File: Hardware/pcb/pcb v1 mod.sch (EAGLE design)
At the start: 36 parts, among them K1 JS-M1-9V-4, K2 JS-M1-9V-4, Q1 32.768kHz 12.5pF, Q6 MOSFET-NCHANNELBSS138, Q7 MOSFET-NCHANNELBSS138, Q8 MOSFET-NCHANNELBSS138, Q9 MOSFET-NCHANNELBSS138, U1 ADP3338AKCZ-3.3RL7

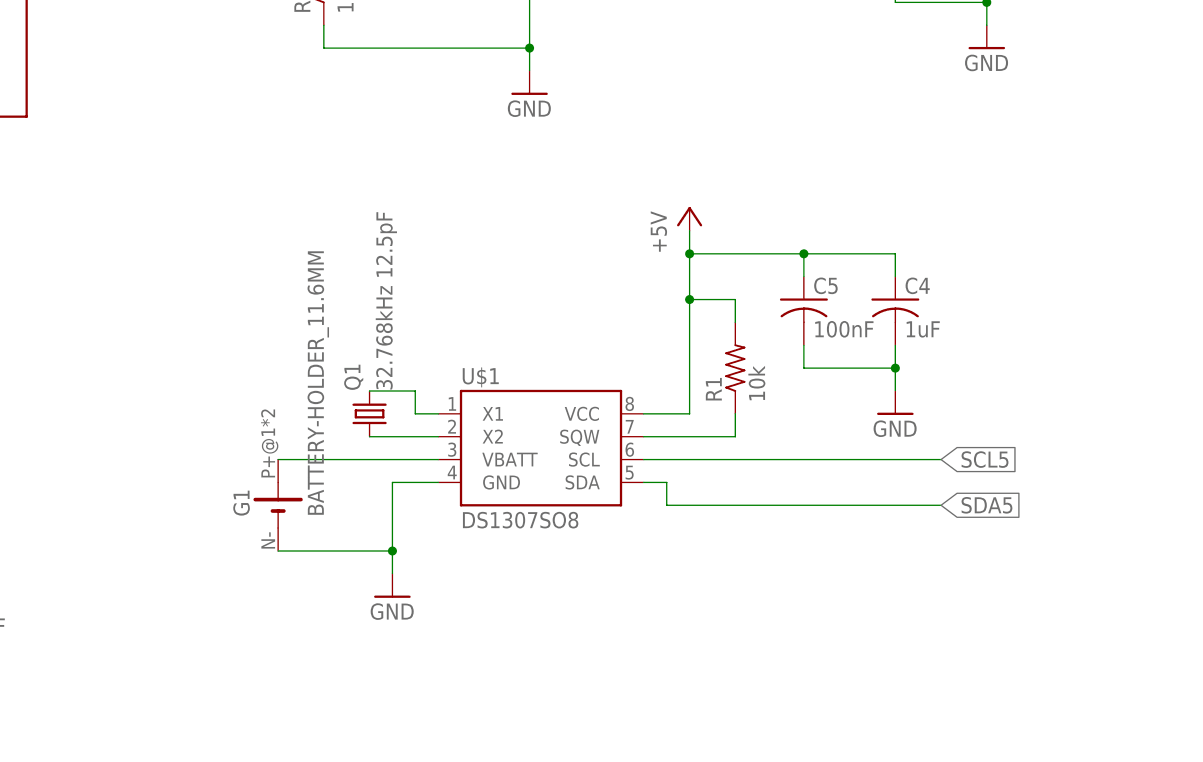
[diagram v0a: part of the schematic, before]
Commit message: Quitar el rtc
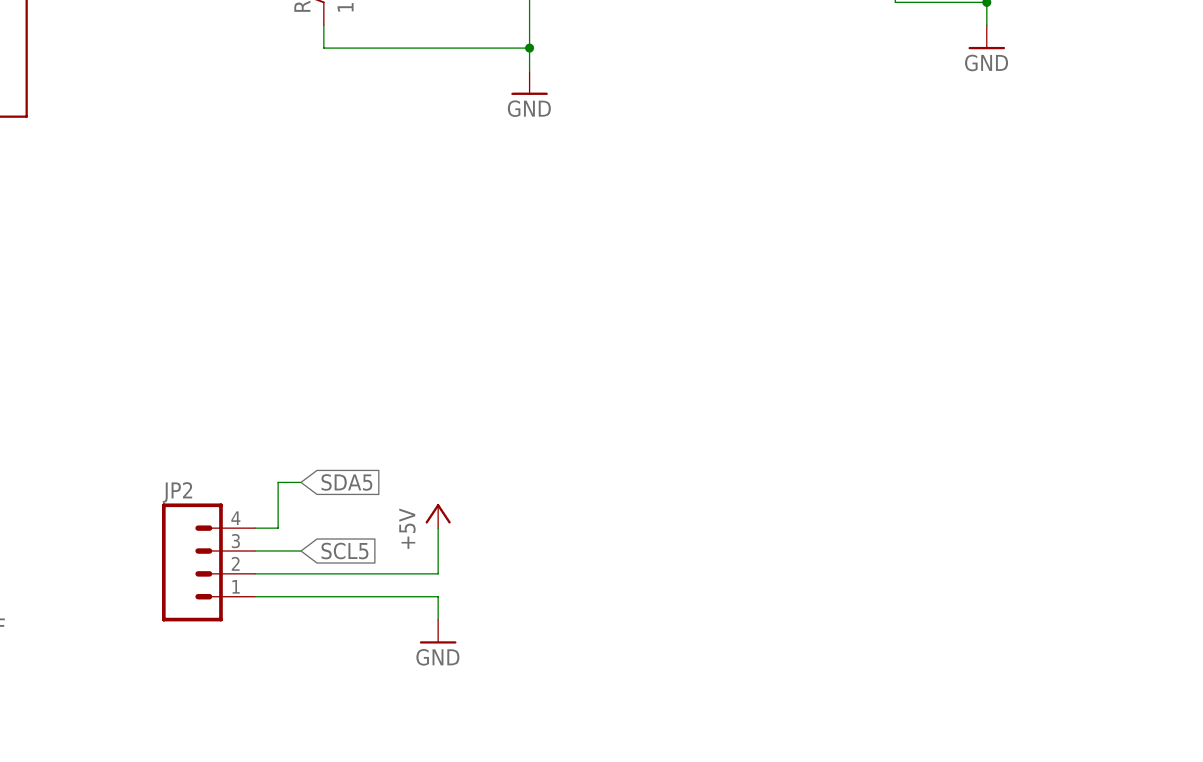
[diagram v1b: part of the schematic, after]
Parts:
- removed C4: 1uF, rcl:C-USC0805
- removed C5: 100nF, rcl:C-USC0805
- removed G1: BATTERY-HOLDER_11.6MM, battery:BATTERY-HOLDER_11.6MM
- removed Q1: 32.768kHz 12.5pF, crystal:CRYSTALTC26H
- removed R1: 10k, rcl:R-US_R0805
- removed U$1: DS1307SO8, SparkFun-FreqCtrl:DS1307SO8
- added JP2: (no value), SparkFun-Connectors:M04PTH
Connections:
- removed net N$2: Q1.2, U$1.X1
- removed net N$3: Q1.1, U$1.X2
- removed net N$4: G1.+, U$1.VBATT
- removed net N$6: R1.1, U$1.SQW
- net +5V: now also JP2.2; no longer C4.1, C5.1, R1.2, U$1.VCC
- net GND: now also JP2.1; no longer C4.2, C5.2, G1.-, U$1.GND
- net SCL5: now also JP2.3; no longer U$1.SCL
- net SDA5: now also JP2.4; no longer U$1.SDA
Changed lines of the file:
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@@
 </classes>
 <parts>
-<part name="G1" library="battery" deviceset="BATTERY-HOLDER_11.6MM" device=""/>
-<part name="Q1" library="crystal" deviceset="CRYSTAL" device="TC26H" value="32.768kHz 12.5pF"/>
 <part name="RFID1" library="partes" deviceset="GROVE-RFID" device=""/>
 <part name="MDL1" library="ESP8266-ESP12E" deviceset="ESP8266-12E" device="ESP8266-ESP12E"/>
@@
 <part name="P+1" library="supply1" deviceset="+5V" device=""/>
 <part name="S1" library="SparkFun-Electromechanical" deviceset="SWITCH-SPDT" device="PTH"/>
-<part name="U$1" library="SparkFun-FreqCtrl" deviceset="DS1307" device="SO8"/>
 <part name="P+2" library="supply1" deviceset="+5V" device=""/>
 <part name="GND3" library="supply1" deviceset="GND" device=""/>
-<part name="R1" library="rcl" deviceset="R-US_" device="R0805" value="10k"/>
 <part name="GND4" library="supply1" deviceset="GND" device=""/>
 <part name="P+6" library="supply1" deviceset="+5V" device=""/>
@@
 <part name="GND8" library="supply1" deviceset="GND" device=""/>
 <part name="GND9" library="supply1" deviceset="GND" device=""/>
-<part name="C4" library="rcl" deviceset="C-US" device="C0805" value="1uF"/>
-<part name="C5" library="rcl" deviceset="C-US" device="C0805" value="100nF"/>
-<part name="GND10" library="supply1" deviceset="GND" device=""/>
 <part name="C6" library="rcl" deviceset="C-US" device="C0805" value="100nF"/>
 <part name="C7" library="rcl" deviceset="C-US" device="C0805" value="100nF"/>
+<part name="JP2" library="SparkFun-Connectors" deviceset="M04" device="PTH"/>
 </parts>
 <sheets>
@@
 </plain>
 <instances>
-<instance part="G1" gate="G$1" x="124.46" y="22.86" rot="R90"/>
-<instance part="Q1" gate="G$1" x="134.62" y="33.02" rot="R90"/>
 <instance part="RFID1" gate="G$1" x="66.04" y="66.04"/>
 <instance part="MDL1" gate="G$1" x="218.44" y="152.4"/>
@@
 <instance part="P+1" gate="1" x="22.86" y="30.48"/>
 <instance part="S1" gate="1" x="10.16" y="20.32"/>
-<instance part="U$1" gate="G$1" x="152.4" y="30.48"/>
-<instance part="P+2" gate="1" x="170.18" y="55.88"/>
-<instance part="GND3" gate="1" x="137.16" y="12.7"/>
-<instance part="R1" gate="G$1" x="175.26" y="38.1" rot="R90"/>
+<instance part="P+2" gate="1" x="142.24" y="22.86"/>
+<instance part="GND3" gate="1" x="142.24" y="7.62"/>
 <instance part="GND4" gate="1" x="55.88" y="40.64"/>
 <instance part="P+6" gate="1" x="55.88" y="81.28"/>
@@
 <instance part="GND8" gate="1" x="241.3" y="76.2"/>
 <instance part="GND9" gate="1" x="203.2" y="73.66"/>
-<instance part="C4" gate="G$1" x="193.04" y="45.72"/>
-<instance part="C5" gate="G$1" x="182.88" y="45.72"/>
-<instance part="GND10" gate="1" x="193.04" y="33.02"/>
 <instance part="C6" gate="G$1" x="193.04" y="86.36"/>
 <instance part="C7" gate="G$1" x="86.36" y="12.7"/>
+<instance part="JP2" gate="G$1" x="116.84" y="15.24"/>
 </instances>
 <busses>
@@
 </segment>
 <segment>
-<pinref part="G1" gate="G$1" pin="-"/>
-<wire x1="124.46" y1="17.78" x2="137.16" y2="17.78" width="0.1524" layer="91"/>
-<wire x1="137.16" y1="17.78" x2="137.16" y2="25.4" width="0.1524" layer="91"/>
-<pinref part="U$1" gate="G$1" pin="GND"/>
-<wire x1="137.16" y1="25.4" x2="142.24" y2="25.4" width="0.1524" layer="91"/>
-<pinref part="GND3" gate="1" pin="GND"/>
-<wire x1="137.16" y1="15.24" x2="137.16" y2="17.78" width="0.1524" layer="91"/>
-<junction x="137.16" y="17.78"/>
-</segment>
-<segment>
 <pinref part="Q6" gate="G$1" pin="S"/>
 <pinref part="GND4" gate="1" pin="GND"/>
@@
 </segment>
 <segment>
-<pinref part="C4" gate="G$1" pin="2"/>
-<pinref part="GND10" gate="1" pin="GND"/>
-<wire x1="193.04" y1="35.56" x2="193.04" y2="38.1" width="0.1524" layer="91"/>
-<pinref part="C5" gate="G$1" pin="2"/>
-<wire x1="193.04" y1="38.1" x2="193.04" y2="40.64" width="0.1524" layer="91"/>
-<wire x1="182.88" y1="40.64" x2="182.88" y2="38.1" width="0.1524" layer="91"/>
-<wire x1="182.88" y1="38.1" x2="193.04" y2="38.1" width="0.1524" layer="91"/>
-<junction x="193.04" y="38.1"/>
+<pinref part="JP2" gate="G$1" pin="1"/>
+<pinref part="GND3" gate="1" pin="GND"/>
+<wire x1="121.92" y1="12.7" x2="142.24" y2="12.7" width="0.1524" layer="91"/>
+<wire x1="142.24" y1="12.7" x2="142.24" y2="10.16" width="0.1524" layer="91"/>
 </segment>
 </net>
@@
 </segment>
 <segment>
-<pinref part="U$1" gate="G$1" pin="VCC"/>
-<pinref part="P+2" gate="1" pin="+5V"/>
-<wire x1="165.1" y1="33.02" x2="170.18" y2="33.02" width="0.1524" layer="91"/>
-<wire x1="170.18" y1="33.02" x2="170.18" y2="45.72" width="0.1524" layer="91"/>
-<pinref part="R1" gate="G$1" pin="2"/>
-<wire x1="170.18" y1="45.72" x2="170.18" y2="50.8" width="0.1524" layer="91"/>
-<wire x1="170.18" y1="50.8" x2="170.18" y2="53.34" width="0.1524" layer="91"/>
-<wire x1="175.26" y1="43.18" x2="175.26" y2="45.72" width="0.1524" layer="91"/>
-<wire x1="175.26" y1="45.72" x2="170.18" y2="45.72" width="0.1524" layer="91"/>
-<junction x="170.18" y="45.72"/>
-<pinref part="C5" gate="G$1" pin="1"/>
-<pinref part="C4" gate="G$1" pin="1"/>
-<wire x1="193.04" y1="48.26" x2="193.04" y2="50.8" width="0.1524" layer="91"/>
-<wire x1="193.04" y1="50.8" x2="182.88" y2="50.8" width="0.1524" layer="91"/>
-<wire x1="182.88" y1="50.8" x2="182.88" y2="48.26" width="0.1524" layer="91"/>
-<wire x1="182.88" y1="50.8" x2="170.18" y2="50.8" width="0.1524" layer="91"/>
-<junction x="182.88" y="50.8"/>
-<junction x="170.18" y="50.8"/>
-</segment>
-<segment>
 <pinref part="P+6" gate="1" pin="+5V"/>
 <wire x1="55.88" y1="78.74" x2="55.88" y2="73.66" width="0.1524" layer="91"/>
@@
 <wire x1="193.04" y1="88.9" x2="193.04" y2="91.44" width="0.1524" layer="91"/>
 <wire x1="193.04" y1="91.44" x2="203.2" y2="91.44" width="0.1524" layer="91"/>
+</segment>
+<segment>
+<pinref part="JP2" gate="G$1" pin="2"/>
+<pinref part="P+2" gate="1" pin="+5V"/>
+<wire x1="121.92" y1="15.24" x2="142.24" y2="15.24" width="0.1524" layer="91"/>
+<wire x1="142.24" y1="15.24" x2="142.24" y2="20.32" width="0.1524" layer="91"/>
 </segment>
 </net>
@@
 </segment>
 </net>
-<net name="N$2" class="0">
-<segment>
-<pinref part="Q1" gate="G$1" pin="2"/>
-<wire x1="134.62" y1="35.56" x2="139.7" y2="35.56" width="0.1524" layer="91"/>
-<wire x1="139.7" y1="35.56" x2="139.7" y2="33.02" width="0.1524" layer="91"/>
-<pinref part="U$1" gate="G$1" pin="X1"/>
-<wire x1="139.7" y1="33.02" x2="142.24" y2="33.02" width="0.1524" layer="91"/>
-</segment>
-</net>
-<net name="N$3" class="0">
-<segment>
-<pinref part="Q1" gate="G$1" pin="1"/>
-<pinref part="U$1" gate="G$1" pin="X2"/>
-<wire x1="134.62" y1="30.48" x2="142.24" y2="30.48" width="0.1524" layer="91"/>
-</segment>
-</net>
-<net name="N$4" class="0">
-<segment>
-<pinref part="G1" gate="G$1" pin="+"/>
-<pinref part="U$1" gate="G$1" pin="VBATT"/>
-<wire x1="124.46" y1="27.94" x2="142.24" y2="27.94" width="0.1524" layer="91"/>
-</segment>
-</net>
-<net name="N$6" class="0">
-<segment>
-<pinref part="R1" gate="G$1" pin="1"/>
-<pinref part="U$1" gate="G$1" pin="SQW"/>
-<wire x1="175.26" y1="33.02" x2="175.26" y2="30.48" width="0.1524" layer="91"/>
-<wire x1="175.26" y1="30.48" x2="165.1" y2="30.48" width="0.1524" layer="91"/>
-</segment>
-</net>
-<net name="SCL5" class="0">
-<segment>
-<pinref part="U$1" gate="G$1" pin="SCL"/>
-<wire x1="165.1" y1="27.94" x2="198.12" y2="27.94" width="0.1524" layer="91"/>
-<label x="198.12" y="27.94" size="1.778" layer="95" xref="yes"/>
-</segment>
-</net>
 <net name="LED5" class="0">
 <segment>
@@
 <pinref part="D3" gate="G$1" pin="DIN"/>
 <wire x1="236.22" y1="91.44" x2="243.84" y2="91.44" width="0.1524" layer="91"/>
-</segment>
-</net>
-<net name="SDA5" class="0">
-<segment>
-<label x="198.12" y="22.86" size="1.778" layer="95" xref="yes"/>
-<pinref part="U$1" gate="G$1" pin="SDA"/>
-<wire x1="167.64" y1="22.86" x2="198.12" y2="22.86" width="0.1524" layer="91"/>
-<wire x1="165.1" y1="25.4" x2="167.64" y2="25.4" width="0.1524" layer="91"/>
-<wire x1="167.64" y1="25.4" x2="167.64" y2="22.86" width="0.1524" layer="91"/>
 </segment>
 </net>
@@
 </segment>
 </net>
+<net name="SDA5" class="0">
+<segment>
+<pinref part="JP2" gate="G$1" pin="4"/>
+<wire x1="121.92" y1="20.32" x2="124.46" y2="20.32" width="0.1524" layer="91"/>
+<wire x1="124.46" y1="20.32" x2="124.46" y2="25.4" width="0.1524" layer="91"/>
+<wire x1="124.46" y1="25.4" x2="127" y2="25.4" width="0.1524" layer="91"/>
+<label x="127" y="25.4" size="1.778" layer="95" xref="yes"/>
+</segment>
+</net>
+<net name="SCL5" class="0">
+<segment>
+<pinref part="JP2" gate="G$1" pin="3"/>
+<wire x1="121.92" y1="17.78" x2="127" y2="17.78" width="0.1524" layer="91"/>
+<label x="127" y="17.78" size="1.778" layer="95" xref="yes"/>
+</segment>
+</net>

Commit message: Modulo reles
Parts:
- removed D1, D2: 1N5819HW, diego:1N5819HW
- removed K1, K2: JS-M1-9V-4, relay:JS-M1-9V-4
- removed Q7, Q8: MOSFET-NCHANNELBSS138, SparkFun-DiscreteSemi:MOSFET-NCHANNELBSS138
- removed R12, R14: 100, rcl:R-US_R0805
- removed R13, R15: 1M, rcl:R-US_R0805
- removed X1, X2: (no value), con-wago-500:W237-103
- added JP3: (no value), SparkFun-Connectors:M04PTH
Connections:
- net RFIDTX5 renamed RFIDTX33
- net SCL5 renamed SCL33
- net SDA5 renamed SDA33
- removed net N$12: D1.A, K11.2, Q7.D
- removed net N$14: Q7.G, R12.2
- removed net N$15: K12.O, X1-3.KL
- removed net N$16: K12.P, X1-2.KL
- removed net N$17: K12.S, X1-1.KL
- removed net N$18: D2.A, K21.2, Q8.D
- removed net N$19: Q8.G, R14.2
- removed net N$20: K22.O, X2-3.KL
- removed net N$21: K22.P, X2-2.KL
- removed net N$22: K22.S, X2-1.KL
- removed net RELE1: R12.1, R13.2
- removed net RELE2: R14.1, R15.2
- new net RELE1-33: JP3.4
- new net RELE2-33: JP3.3
- net +5V: now also JP3.2; no longer D1.C, D2.C, K11.1, K21.1
- net GND: now also JP3.1; no longer Q7.S, Q8.S, R13.1, R15.1
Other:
- moved on the sheet: C3, C6, D3, MDL1, Q6, Q9, R10, R11, R16, R17, RFID1, SG1

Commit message: esp y atmega328
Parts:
- removed C3: 1uF, rcl:C-USC0805
- removed C6: 100nF, rcl:C-USC0805
- removed D3: (no value), SparkFun-LED:WS2812B
- added C10, C9: 22pF, rcl:C-USC1206
- added C11, C8: 0.1uF, rcl:C-USC0805
- added D1: LED-RGB-CC-THRUCLEAR, SparkFun-LED:LED-RGB-CC-THRUCLEAR
- added J3: AVR_SPI_PRG_6PTH, SparkFun-Connectors:AVR_SPI_PRG_6PTH
- added JP4, JP5, JP6, JP7: (no value), SparkFun-Connectors:M03PTH
- added R1, R12, R2, R3, R5, R6, R7: 10k, rcl:R-US_R0805
- added R13, R9: 100R, rcl:R-US_R0805
- added R4: 100K, rcl:R-US_R0805
- added R8: 160R, rcl:R-US_R0805
- added U3: ATMEGA328P, SparkFun-DigitalIC:ATMEGA328_SMT
- added Y1: 16Mhz, SparkFun-FreqCtrl:CRYSTALHC49US
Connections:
- net RELE2-33 renamed RELE1
- net RFIDTX33 renamed RFID_TX
- removed net LED5: D3.DIN
- removed net RELE1-33: JP3.4
- removed net SCL33: JP2.3
- removed net SDA33: JP2.4
- new net ESP_RX_33: JP5.1, JP5.3
- new net ESP_TX_33: JP4.1, JP4.3
- new net N$10: D1.RED_CATHODE, R8.2
- new net N$11: C9.1, U3.PB6(XTAL1/TOSC1), Y1.1
- new net N$12: C10.1, U3.PB7(XTAL2/TOSC2), Y1.2
- new net N$14: C11.1, U3.AREF
- new net N$15: D1.GREEN_CATHODE, R9.2
- new net N$16: D1.BLUE_CATHODE, R13.2
- new net N$17: J3.3, U3.PB5(SCK)
- new net N$18: J3.1, U3.PB4(MISO)
- new net N$19: J3.4, U3.PB3(MOSI/OC2)
- new net N$2: MDL1.CH_PD, R5.1
- new net N$20: JP6.2, R12.2
- new net N$3: MDL1.GPIO2, R7.1
- new net N$39: J3.5, R4.2, U3.PC6(/RESET)
- new net N$4: MDL1.GPIO0, R12.1
- new net N$5: MDL1.GPIO15, R6.2
- new net N$6: JP5.2, MDL1.RXD
- new net N$8: JP4.2, MDL1.TXD
- new net N$9: JP7.1, MDL1.REST, R3.1
- new net RELE2: JP3.2
- new net SCL: JP2.3, R1.1
- new net SDA: JP2.4, R2.1
- net +3V3: now also JP6.3, MDL1.VCC, R3.2, R5.2, R7.2
- net +5V: now also C8.1, J3.2, JP3.4, R1.2, R2.2, R4.1, U3.AVCC, U3.VCC@1, U3.VCC@2; no longer C3.1, C6.1, D3.VDD, JP3.2
- net GND: now also C10.2, C11.2, C8.2, C9.2, J3.6, JP6.1, JP7.2, MDL1.GND, R6.1, U3.AGND, U3.GND@1, U3.GND@2; no longer C3.2, C6.2, D3.VSS
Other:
- moved on the sheet: JP3, MDL1

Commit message: Esquematico completo
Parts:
- removed Q6, Q9: MOSFET-NCHANNELBSS138, SparkFun-DiscreteSemi:MOSFET-NCHANNELBSS138
- removed R11, R17: 1M, rcl:R-US_R0805
- removed R16: 100, rcl:R-US_R0805
- added C3: 1uF, rcl:C-USC1206
- added C4, C5, C6: 100nF, rcl:C-USC0805
- added LVLSHF2: LEVELSHIFTER4, partes:LEVELSHIFTER4
- added Q1: 2N3906, transistor-pnp:2N3906
- added R14: 10k, rcl:R-US_R0805
- C1: value 1uF -> 10uF; device rcl:CPOL-US150CLZ-1010 -> rcl:CPOL-USE2.5-6
- C11, C8: value 0.1uF -> 100nF
- C2: value 1uF -> 100nF; device rcl:CPOL-US150CLZ-1010 -> rcl:C-USC0805
- C7: value 100nF -> 10uF; device rcl:C-USC0805 -> rcl:CPOL-USE2.5-6
- R10: value 100 -> 10k
- R8: device rcl:R-US_R0805 -> rcl:R-US_R1206
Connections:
- removed net N$13: Q6.G, R10.2
- removed net N$24: Q9.D, SG1.2
- removed net RFIDPW: R10.1, R11.2
- new net LED_B: R13.1, U3.PD6(AIN0)
- new net LED_G: R9.1, U3.PB2(SS/OC1B)
- new net LED_R: R8.1, U3.PB1(OC1A)
- new net N$21: LVLSHF2.HV1, U3.PD0(RXD)
- new net N$22: LVLSHF2.HV2, U3.PD1(TXD)
- new net RFID_PW: R10.1, U3.PD5(T1)
- net +3V3: now also C1.+, C2.1, C3.1, C4.1, LVLSHF2.LV; no longer C2.+, C7.1
- net +5V: now also C5.1, C6.1, C7.+, LVLSHF2.HV, Q1.E, R14.2; no longer C1.+, RFID1.VCC, SG1.1
- net BUZZER: now also SG1.1, U3.PC0(ADC0); no longer R16.1, R17.2
- net ESP_RX_33: now also LVLSHF2.LV2
- net ESP_TX_33: now also LVLSHF2.LV1
- net GND: now also C2.2, C3.2, C4.2, C5.2, C6.2, C7.-, D1.CATHODE, LVLSHF2.GND, RFID1.GND, SG1.2; no longer C2.-, C7.2, Q6.S, Q9.S, R11.1, R17.1
- net N$23: now also Q1.C, RFID1.VCC; no longer Q9.G, R16.2
- net N$7: now also Q1.B, R10.2, R14.1; no longer Q6.D, RFID1.GND
- net RELE1: now also U3.PC1(ADC1)
- net RELE2: now also U3.PC2(ADC2)
- net RFID_TX: now also U3.PD2(INT0)
- net SCL: now also U3.PC5(ADC5/SCL)
- net SDA: now also U3.PC4(ADC4/SDA)
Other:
- moved on the sheet: C1, JP3, R10, SG1
